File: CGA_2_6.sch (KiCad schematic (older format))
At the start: 2 parts, among them U36 74LS244, U37 74LS374

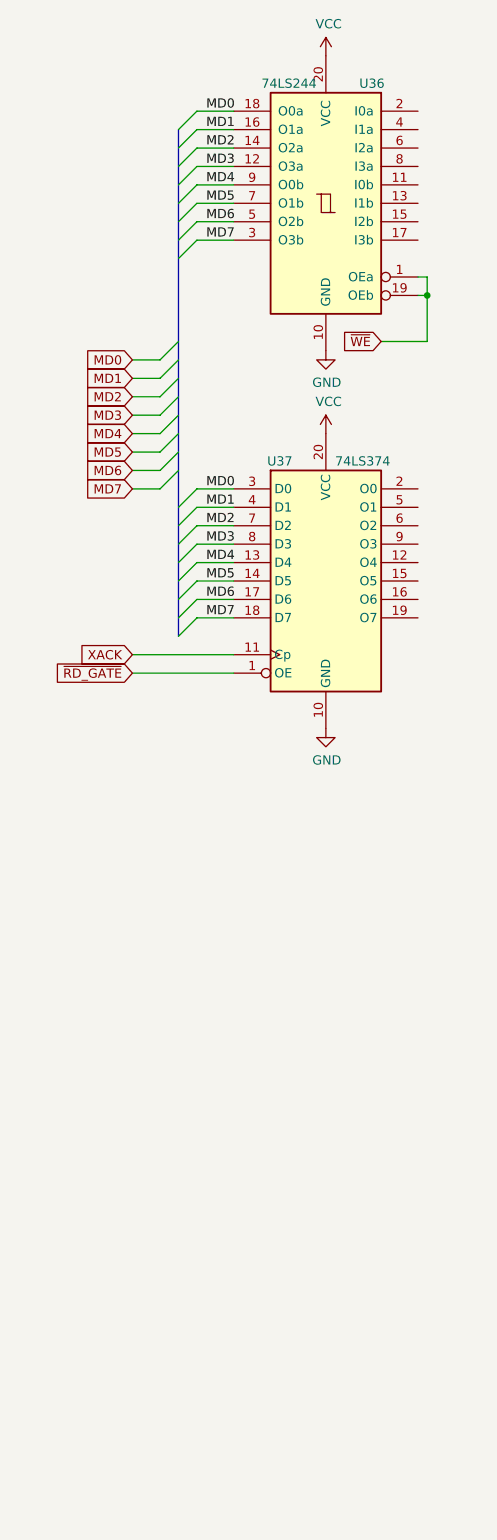
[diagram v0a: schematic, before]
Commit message: More drawings of sheet 2
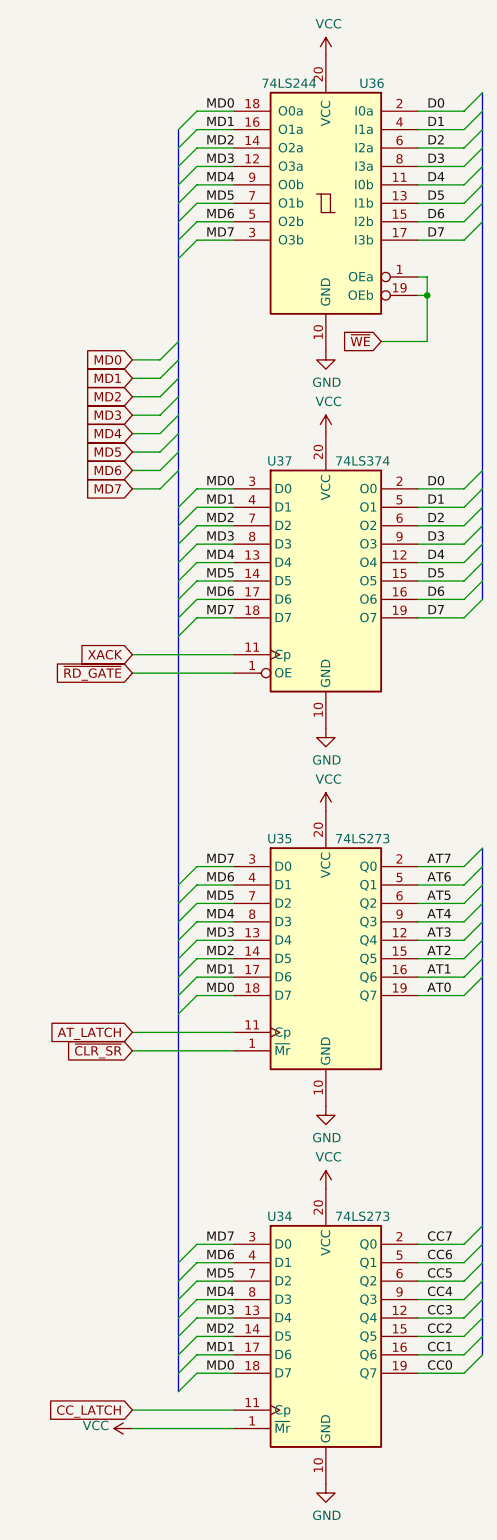
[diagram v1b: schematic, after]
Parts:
- added U34, U35: 74LS273, Package_DIP:DIP-20_W7.62mm_LongPads, symbol 74xx:74LS273
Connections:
- net GND: now also U34.10 (GND), U35.10 (GND)
- net MD0: now also U34.18 (D7), U35.18 (D7)
- net MD1: now also U34.17 (D6), U35.17 (D6)
- net MD2: now also U34.14 (D5), U35.14 (D5)
- net MD3: now also U34.13 (D4), U35.13 (D4)
- net MD4: now also U34.8 (D3), U35.8 (D3)
- net MD5: now also U34.7 (D2), U35.7 (D2)
- net MD6: now also U34.4 (D1), U35.4 (D1)
- net MD7: now also U34.3 (D0), U35.3 (D0)
- net VCC: now also U34.1 (~Mr), U34.20 (VCC), U35.20 (VCC)
- net D4: now reaches U36.11 (I0b)
- net D4: now also U37.12 (O4)
- net D5: now reaches U36.13 (I1b)
- net D5: now also U37.15 (O5)
- net D6: now reaches U36.15 (I2b)
- net D6: now also U37.16 (O6)
- net D7: now reaches U36.17 (I3b)
- net D7: now also U37.19 (O7)
- net D0: now reaches U36.2 (I0a)
- net D0: now also U37.2 (O0)
- net D1: now reaches U36.4 (I1a)
- net D1: now also U37.5 (O1)
- net D2: now reaches U36.6 (I2a)
- net D2: now also U37.6 (O2)
- net D3: now reaches U36.8 (I3a)
- net D3: now also U37.9 (O3)
- new net AT0: U35.19 (Q7)
- new net AT1: U35.16 (Q6)
- new net AT2: U35.15 (Q5)
- new net AT3: U35.12 (Q4)
- new net AT4: U35.9 (Q3)
- new net AT5: U35.6 (Q2)
- new net AT6: U35.5 (Q1)
- new net AT7: U35.2 (Q0)
- new net AT_LATCH: U35.11 (Cp)
- new net CC0: U34.19 (Q7)
- new net CC1: U34.16 (Q6)
- new net CC2: U34.15 (Q5)
- new net CC3: U34.12 (Q4)
- new net CC4: U34.9 (Q3)
- new net CC5: U34.6 (Q2)
- new net CC6: U34.5 (Q1)
- new net CC7: U34.2 (Q0)
- new net CC_LATCH: U34.11 (Cp)
- new net ~CLR_SR: U35.1 (~Mr)

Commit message: More sheet 2
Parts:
- added U24: 74LS244, Package_DIP:DIP-20_W7.62mm_LongPads, symbol 74xx:74LS244
- added U39: 74LS174, Package_DIP:DIP-16_W7.62mm_LongPads, symbol 74xx:74LS174
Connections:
- net D0: now also U24.3 (O3b), U39.3 (D0)
- net D1: now also U24.5 (O2b), U39.4 (D1)
- net D2: now also U24.7 (O1b), U39.6 (D2)
- net D3: now also U24.9 (O0b), U39.11 (D3)
- net D4: now also U39.13 (D4)
- net D5: now also U39.14 (D5)
- net GND: now also U24.10 (GND), U39.8 (GND)
- net VCC: now also U24.20 (VCC), U39.16 (VCC)
- new net BACKGROUND_I: U39.12 (Q4)
- new net COLOR_SEL: U39.15 (Q5)
- new net LPEN_STR: U24.15 (I2b)
- new net OVERSCAN_B: U39.2 (Q0)
- new net OVERSCAN_G: U39.5 (Q1)
- new net OVERSCAN_I: U39.10 (Q3)
- new net OVERSCAN_R: U39.7 (Q2)
- new net V_SYNC_DLY: U24.11 (I0b)
- new net ~DISPEN: U24.17 (I3b)
- new net ~LPEN_SW: U24.13 (I1b)
- new net ~RESET: U39.1 (~Mr)
- new net ~SEL_2: U39.9 (Cp)
- new net ~STATUS_SEL: U24.19 (OEb)
- no-connect marks 0 -> 9

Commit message: More sheet 2
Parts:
- added U32: 74LS166, Package_DIP:DIP-16_W7.62mm_LongPads, symbol 74xx:74LS166
- added U33: 27C256, Package_DIP:DIP-28_W15.24mm_LongPads, symbol Memory_EPROM:27C256
- added U68: 74LS86, Package_DIP:DIP-14_W7.62mm_LongPads, symbol 74xx:74LS86
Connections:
- net CC0: now also U33.7 (A3)
- net CC1: now also U33.6 (A4)
- net CC2: now also U33.5 (A5)
- net CC3: now also U33.4 (A6)
- net CC4: now also U33.3 (A7)
- net CC5: now also U33.25 (A8)
- net CC6: now also U33.24 (A9)
- net CC7: now also U33.21 (A10)
- net GND: now also U32.1 (Ds), U32.6 (CE), U32.8 (GND), U33.14 (GND), U33.22 (~OE)
- net VCC: now also U32.16 (VCC), U33.1 (VPP), U33.2 (A12), U33.23 (A11), U33.26 (A13), U33.27 (A14), U33.28 (VCC)
- net ~CLR_SR: now also U32.9 (Clr)
- new net: U32.2 (A), U33.11 (D0)
- new net: U32.3 (B), U33.12 (D1)
- new net: U32.4 (C), U33.13 (D2)
- new net: U32.5 (D), U33.15 (D3)
- new net: U32.10 (E), U33.16 (D4)
- new net: U32.11 (F), U33.17 (D5)
- new net: U32.12 (G), U33.18 (D6)
- new net: U32.14 (H), U33.19 (D7)
- new net: U33.20 (~CE), U68.11
- new net: U68.12, U68.8
- new net CHG_DOTS: U32.13 (Qh)
- new net DOT_CLK: U32.7 (Clk)
- new net Q4: U68.10
- new net RA0: U33.10 (A0)
- new net RA1: U33.9 (A1)
- new net RA2: U33.8 (A2)
- new net RESET: U68.13
- new net SL: U32.15 (PE)
- new net ~LCLK: U68.9

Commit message: More  sheet 2
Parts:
- added U7, U?: 74LS166, Package_DIP:DIP-16_W7.62mm_LongPads, symbol 74xx:74LS166
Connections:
- net GND: now also U7.1 (Ds), U7.6 (CE), U7.8 (GND), U?.1 (Ds), U?.6 (CE), U?.8 (GND)
- net VCC: now also U7.16 (VCC), U?.16 (VCC)
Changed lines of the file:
@@
 Wire Wire Line
 	8100 5800 8250 5800
+Text GLabel 8250 5800 2    50   Output ~ 0
+CHG_DOTS
+Wire Bus Line
+	4400 5200 8850 5200
+Wire Bus Line
+	8850 5200 8850 5800
+Connection ~ 4400 5200
+$Comp
+L 74xx:74LS166 U7
+U 1 1 60DECB37
+P 10450 4900
+F 0 "U7" H 10150 5750 50  0000 L CNN
+F 1 "74LS166" H 10500 5750 50  0000 L CNN
+F 2 "Package_DIP:DIP-16_W7.62mm_LongPads" H 10450 4900 50  0001 C CNN
+F 3 "http://www.ti.com/lit/gpn/sn74LS166" H 10450 4900 50  0001 C CNN
+	1    10450 4900
+	1    0    0    -1
+$EndComp
+$Comp
+L power:VCC #PWR?
+U 1 1 60DEFE94
+P 10450 3900
+F 0 "#PWR?" H 10450 3750 50  0001 C CNN
+F 1 "VCC" H 10465 4073 50  0000 C CNN
+F 2 "" H 10450 3900 50  0001 C CNN
+F 3 "" H 10450 3900 50  0001 C CNN
+	1    10450 3900
+	1    0    0    -1
+$EndComp
+$Comp
+L power:GND #PWR?
+U 1 1 60DF0971
+P 10450 5900
+F 0 "#PWR?" H 10450 5650 50  0001 C CNN
+F 1 "GND" H 10455 5727 50  0000 C CNN
+F 2 "" H 10450 5900 50  0001 C CNN
+F 3 "" H 10450 5900 50  0001 C CNN
+	1    10450 5900
+	1    0    0    -1
+$EndComp
+Wire Wire Line
+	9950 4200 9500 4200
+Wire Wire Line
+	9500 4200 9500 5400
+Wire Wire Line
+	9950 5400 9500 5400
+Connection ~ 9500 5400
+Wire Wire Line
+	9500 5400 9500 5850
+$Comp
+L power:GND #PWR?
+U 1 1 60E0DEFD
+P 9500 5850
+F 0 "#PWR?" H 9500 5600 50  0001 C CNN
+F 1 "GND" H 9505 5677 50  0000 C CNN
+F 2 "" H 9500 5850 50  0001 C CNN
+F 3 "" H 9500 5850 50  0001 C CNN
+	1    9500 5850
+	1    0    0    -1
+$EndComp
+$Comp
+L 74xx:74LS166 U?
+U 1 1 60E20D0C
+P 10450 7500
+F 0 "U?" H 10150 8350 50  0000 L CNN
+F 1 "74LS166" H 10500 8350 50  0000 L CNN
+F 2 "Package_DIP:DIP-16_W7.62mm_LongPads" H 10450 7500 50  0001 C CNN
+F 3 "http://www.ti.com/lit/gpn/sn74LS166" H 10450 7500 50  0001 C CNN
+	1    10450 7500
+	1    0    0    -1
+$EndComp
+$Comp
+L power:VCC #PWR?
+U 1 1 60E20F7C
+P 10450 6500
+F 0 "#PWR?" H 10450 6350 50  0001 C CNN
+F 1 "VCC" H 10465 6673 50  0000 C CNN
+F 2 "" H 10450 6500 50  0001 C CNN
+F 3 "" H 10450 6500 50  0001 C CNN
+	1    10450 6500
+	1    0    0    -1
+$EndComp
+$Comp
+L power:GND #PWR?
+U 1 1 60E20F86
+P 10450 8500
+F 0 "#PWR?" H 10450 8250 50  0001 C CNN
+F 1 "GND" H 10455 8327 50  0000 C CNN
+F 2 "" H 10450 8500 50  0001 C CNN
+F 3 "" H 10450 8500 50  0001 C CNN
+	1    10450 8500
+	1    0    0    -1
+$EndComp
+Wire Wire Line
+	9950 6800 9500 6800
+Wire Wire Line
+	9500 6800 9500 8000
+Wire Wire Line
+	9950 8000 9500 8000
+Connection ~ 9500 8000
+Wire Wire Line
+	9500 8000 9500 8450
+$Comp
+L power:GND #PWR?
+U 1 1 60E20F95
+P 9500 8450
+F 0 "#PWR?" H 9500 8200 50  0001 C CNN
+F 1 "GND" H 9505 8277 50  0000 C CNN
+F 2 "" H 9500 8450 50  0001 C CNN
+F 3 "" H 9500 8450 50  0001 C CNN
+	1    9500 8450
+	1    0    0    -1
+$EndComp
 Wire Bus Line
 	5800 1150 5800 4050
@@
 Wire Bus Line
 	1700 1400 1700 8250
-Text GLabel 8250 5800 2    50   Output ~ 0
-CHG_DOTS
 $EndSCHEMATC

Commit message: More sheet 2
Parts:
- gave numbers to parts that had none: 1
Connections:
- net AT0: now also U7.2 (A)
- net AT1: now also U7.2 (A)
- net AT2: now also U7.3 (B)
- net AT3: now also U7.3 (B)
- net AT4: now also U7.4 (C)
- net AT5: now also U7.4 (C)
- net AT6: now also U7.5 (D)
- net AT7: now also U7.5 (D)
- net CC0: now also U7.10 (E)
- net CC1: now also U7.10 (E)
- net CC2: now also U7.11 (F)
- net CC3: now also U7.11 (F)
- net CC4: now also U7.12 (G)
- net CC5: now also U7.12 (G)
- net CC6: now also U7.14 (H)
- net CC7: now also U7.14 (H)
- net DOT_CLK: now also U7.7 (Clk), U7.7 (Clk)
- net SL: now also U7.15 (PE), U7.15 (PE)
- net ~CLR_SR: now also U7.9 (Clr), U7.9 (Clr)
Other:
- moved on the sheet: U7
